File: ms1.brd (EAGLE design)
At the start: 160 x 100 mm, 119 parts, among them IC1 MAX3232EUE, J1 POWERPOLE_POWER25A, J10 Radio, J11 4-PIN-MOLEX, J12 4-PIN-MOLEX, J13 ADC2, J14 ADC2, J2 ON, J3 LED-EN, J4 RS232, J5 2-PIN-MOLEX, J6 ADC1, J7 I2C, J8 ADC2, J9 TTL_SERIAL, Q1 DMG6602SVT, Q2 DMG6602SVT, Q3 DMG6602SVT, Q4 DMG6602SVT, U1 LT1934ES6TRMPBF, U2 LT1934ES6TRMPBF, U3 DS3231SN, U4 ISL3179EIBZ, X1 KUSBVX-BS1N

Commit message: now all routed :)
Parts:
- removed C27, C29: (no value), resistor:C0805
- removed C28, C30: (no value), resistor:B/3528-21R
- removed J9: TTL_SERIAL, farnell-parts:5-MOLEX
- removed JP16, JP8: (no value), SparkFun-Passives:SJ_2S-NO
- removed L7, L8: 10mH, resistor:L3230M
- removed LED12: RADIO, led:CHIP-LED0805
- removed LED13: RADIO_EN, led:CHIP-LED0805
- removed LED14: BAT_EN, led:CHIP-LED0805
- removed LED15: SENSE_EN, led:CHIP-LED0805
- removed R30: 56, resistor:R0805
- removed R31: 100K, resistor:R0805
- removed R32, R33: 1K, resistor:R0805
- removed U$1: BUTTON_CELL_NEW, gumsense:CR2016
- removed U$2: Z1, z1:Z1
- removed U$4: TXS0108E, basestation:TSSOP20
- removed U$7: MCF0805, farnell-parts:0805
- added C17: (no value), resistor:C0805
- added C18: (no value), resistor:B/3528-21R
- added C22: 0.1uF, resistor:A/3216-18W
- added C23: 100nF, resistor:C0805
- added F1, F2, F3, F4, F5, F6, F7, F8: MCF0805, farnell-parts:0805
- added JP3: (no value), SparkFun-Passives:SJ_2S
- added JP4: (no value), jumper:JP2
- added L1: 47uH, farnell-parts:1048
- added L2: 20uH, rcl:6000-XXXX-RC
- added LED3: RAIN, led:CHIP-LED0805
- added LED4: 12V, led:CHIP-LED0805
- added LED5: 3V3, led:CHIP-LED0805
- added LED6: SENSE, led:CHIP-LED0805
- added R13: 100K, resistor:R0805
- added R15, R16: 56, resistor:R0805
- added R17: 560, resistor:R0805
- added U$8: CC1120-HEADER-SMT, CC11x:CC1120-HEADERS-SMT
- C1: value 2200uF -> 2.2uF; device rcl:E5-13 -> resistor:C0805
- C10: value 10pF -> 1uF
- C11: value 68uF -> 100nF; device rcl:PANASONIC_E -> resistor:C0805
- C12: value 330uF -> 2.2uF; device rcl:E5-8,5 -> resistor:C0805
- C13: value 100nF -> 0.22uF
- C14: value 100nF -> 10pF; device glacsweb:C0805 -> resistor:C0805
- C15: value 0.1uF -> 68uF; device resistor:A/3216-18W -> rcl:PANASONIC_E
- C16: value 0.1uF -> 330uF; device resistor:A/3216-18W -> rcl:E5-8,5
- C2: value 2.2uF -> 0.22uF
- C20: value 0.1uF -> 100nF; device resistor:A/3216-18W -> glacsweb:C0805
- C24, C25: value 100nF -> 0.1uF; device resistor:C0805 -> resistor:A/3216-18W
- C3: value 0.22uF -> 2200uF; device resistor:C0805 -> rcl:E5-13
- C5: value 1uF -> 100uF; device resistor:C0805 -> rcl:PANASONIC_E
- C6: value 100uF -> 330uF; device rcl:PANASONIC_E -> rcl:E5-8,5
- C7: value 330uF -> (none); device rcl:E5-8,5 -> resistor:C0805
- C8: value 2.2uF -> (none); device resistor:C0805 -> resistor:B/3528-21R
- C9: value 0.22uF -> 100nF
- J10: value Radio -> RS485; device farnell-parts:5-MOLEX -> farnell-parts:4-MOLEX
- J11: value 4-PIN-MOLEX -> I2C; device farnell-parts:4-MOLEX -> farnell-parts:5-MOLEX
- J12: value 4-PIN-MOLEX -> TTL_SERIAL
- J13: value ADC2 -> Radio; device farnell-parts:3-MOLEX -> farnell-parts:5-MOLEX
- J14: value ADC2 -> RS232; device farnell-parts:3-MOLEX -> farnell-parts:4-MOLEX
- J2: value ON -> RAIN
- J3: value LED-EN -> ADC1; device farnell-parts:2-MOLEX -> farnell-parts:3-MOLEX
- J4: value RS232 -> ON; device farnell-parts:5-MOLEX -> farnell-parts:2-MOLEX
- J5: value 2-PIN-MOLEX -> D1; device farnell-parts:2-MOLEX -> farnell-parts:3-MOLEX
- J6: value ADC1 -> D2
- J7: value I2C -> ADC2; device farnell-parts:5-MOLEX -> farnell-parts:3-MOLEX
- J8: value ADC2 -> LED-EN; device farnell-parts:3-MOLEX -> farnell-parts:2-MOLEX
- JP1: device SparkFun-Passives:SJ_2S -> SparkFun-Passives:SJ_2S-NO
- JP2: device jumper:JP2 -> SparkFun-Passives:SJ_2S-NO
- L3: value 47uH -> 10mH; device farnell-parts:1048 -> resistor:L3230M
- L4: value 20uH -> 10mH; device rcl:6000-XXXX-RC -> resistor:L3230M
- LED10: value SENSE -> BAT_EN
- LED11: value SENSE_5V -> SENSE_EN
- LED7: value D7 -> 5V
- LED8: value 12V -> RADIO
- LED9: value 3V3 -> RADIO_EN
- R10, R8: value 56 -> 100K
- R14, R26: value 100K -> 56
- R19: value 560 -> 56
- R2: value 100K -> 1M
- R20: value 56 -> 1M
- R21: value 56 -> 332K
- R22: value 100K -> 150
- R23: value 1M -> 56
- R24: value 332K -> 56
- R25: value 150 -> 56
- R27, R29: value 56 -> 1K
- R28: value 56 -> 47K
- R3: value 100K -> 604K
- R4: value 51K -> 100K
- R5: value 1M -> 100K
- R6: value 604K -> 100K
- R7: value 47K -> 100K
- R9: value 100K -> 51K
- U$3: value CC1120-HEADER-SMT -> BUTTON_CELL_NEW; device CC11x:CC1120-HEADERS-SMT -> gumsense:CR2016
- U$5: value MCF0805 -> Z1; device farnell-parts:0805 -> z1:Z1
- U$6: value MCF0805 -> TXS0108E; device farnell-parts:0805 -> basestation:TSSOP20
- moved J5 377.9 mm to (90.0, 95.2), turned to 180 degrees
- moved J14 348.8 mm to (77.2, 5.97)
- moved J6 346.4 mm to (90.0, 89.0), turned to 180 degrees
- moved LED11 327.7 mm to (92.5, 26.5)
- moved JP2 327.1 mm to (85.0, 78.4), turned to 180 degrees
- moved U$6 324.4 mm to (64.4, 16.3), turned to 90 degrees
- moved J12 315.8 mm to (66.0, 5.97)
- moved U4 314.1 mm to (89.3, 17.9), turned to 270 degrees
- moved LED1 309.9 mm to (96.9, 94.7), turned to 180 degrees
- moved LED2 303.4 mm to (96.9, 88.8)
- moved C20 301.7 mm to (96.0, 17.7), turned to 90 degrees
- moved J8 297.2 mm to (55.0, 6.10)
- moved R7 292.7 mm to (55.9, 21.0), turned to 180 degrees
- moved C14 292.4 mm to (72.4, 68.7)
- moved C21 291.5 mm to (82.3, 16.1), turned to 270 degrees
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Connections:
- new net N$11: F4.1, J12.4
- new net N$18: F1.2, J3.1
- new net N$19: F2.2, J7.1
- new net N$21: F7.2, J6.1
- new net N$22: F8.2, J5.1
- net 232_RX: now also U$6.3; no longer U$4.3
- net 232_TX: now also U$6.6; no longer U$4.6
- net 323_3V3: now also C23.2, JP4.3; no longer C19.2, JP2.3
- net 485_3V3: now also C20.1, JP4.1, R27.2; no longer C14.1, JP2.1, R32.2
- net 485_RX: now also U$6.1; no longer U$4.1
- net 485_TX: now also U$6.5; no longer U$4.5
- net ADC_1: now also J3.2, U$5.A16; no longer J6.2, U$2.A16
- net ADC_2: now also J7.2, U$5.A9; no longer J8.2, U$2.A9
- net ADC_3V3: now also U$5.A14, U$5.A4; no longer U$2.A14, U$2.A4
- net ADC_7: now also C10.1, R8.1, R9.2, U$5.A6; no longer C5.1, R3.1, R4.2, U$2.A6
- net AGND: now also C10.2, J3.3, J7.3, R9.1, U$5.A1, U$5.A11, U$5.A12, U$5.A2; no longer C5.2, J6.3, J8.3, R4.1, U$2.A1, U$2.A11, U$2.A12, U$2.A2
- net BATV_EN: now also JP3.2, R25.2, R4.2; no longer JP1.2, R1.2, R29.2
- net DC_IN: now also J4.2, R5.2; no longer J2.2, R2.2
- net DIO_1: now also J5.2, R14.2, U$5.C51; no longer J13.2, R8.2, U$2.C46, U$2.C51
- net DIO_2: now also J6.2, R15.2, U$5.C46; no longer J14.2, R10.2
- net GND: now also C1.2, C12.2, C15.-, C16.-, C17.2, C18.-, C20.2, C23.1, C24.-, C25.+, C3.-, C5.-, C7.2, C8.-, C9.2, J10.1, J14.1, J5.3, J6.3, J8.1, L4.2, R10.1, R21.1, R3.1, R4.1, U$3.GND, U$5.B24, U$5.C39, U$6.11; no longer C1.-, C11.-, C12.-, C13.1, C14.2, C2.2, C20.-, C21.+, C24.2, C27.2, C28.-, C29.2, C30.-, C7.-, C8.2, J13.3, J14.3, J3.1, J4.1, J7.1, J9.1, L8.2, R22.1, R24.1, R31.1, R9.1, U$1.GND, U$2.B24, U$2.C39, U$4.11
- net LGND: now also J8.2, LED3.C, LED4.C, LED5.C, LED6.C; no longer J3.2, LED12.C, LED13.C, LED14.C, LED15.C
- net N$1: now also J4.1; no longer J2.1
- net N$10: now also R27.1; no longer R32.1
- net N$107: now also C5.+, L1.2, L2.1, R2.2; no longer C6.+, L3.2, L4.1, R5.2
- net N$108: now also LED8.A, R23.1; no longer LED12.A, R27.1
- net N$109: now also LED7.A, R22.1; no longer LED11.A, R25.1
- net N$110: now also LED6.A, R19.1; no longer LED10.A, R21.1
- net N$111: now also LED5.A, R18.1; no longer LED9.A, R20.1
- net N$117: now also C2.1; no longer C3.1
- net N$118: now also R2.1, R3.2; no longer R5.1, R6.2
- net N$12: now also R5.1; no longer R2.1
- net N$13: now also C6.+, C7.1, C8.+, JP1.2, L2.2; no longer C29.1, C30.+, C7.+, JP16.2, L4.2
- net N$14: now also C16.+, C17.1, C18.+, JP2.1; no longer C12.+, C27.1, C28.+, JP8.1
- net N$15: now also LED9.A, R24.1; no longer LED13.A, R28.1
- net N$16: now also LED3.A, R16.1; no longer LED7.A, R18.1
- net N$17: now also F6.1, J14.4; no longer J12.4, U$6.1
- net N$2: now also LED4.A, R17.1; no longer LED8.A, R19.1
- net N$20: now also R15.1; no longer R10.1
- net N$23: now also R14.1; no longer R8.1
- net N$24: now also C9.1, L3.2, Q2.P$4; no longer C24.1, L7.2, Q3.P$4
- net N$25: now also Q3.P$3, Q3.P$6; no longer Q2.P$3, Q2.P$6
- net N$26: now also F3.1, J2.1; no longer J5.1, U$7.1
- net N$3: now also C13.2; no longer C9.2
- net N$4: now also C13.1; no longer C9.1
- net N$5: now also C14.2, R20.1, R21.2; no longer C10.2, R23.1, R24.2
- net N$50: now also LED10.A, R25.1; no longer LED14.A, R29.1
- net N$51: now also LED11.A, R26.1; no longer LED15.A, R30.1
- net N$59: now also C22.-; no longer C16.-
- net N$6: now also C14.1, C15.+, R20.2; no longer C10.1, C11.+, R23.2
- net N$7: now also Q2.P$3, Q2.P$6, R7.1; no longer Q3.P$3, Q3.P$6, R14.1
- net N$70: now also R13.1; no longer R26.1
- net N$78: now also C2.2, L1.1; no longer C3.2, L3.1
- net N$8: now also R28.1, U$6.10; no longer R7.1, U$4.10
- net N$80: now also C22.+; no longer C16.+
- net N$81: now also C21.-; no longer C15.-
- net N$85: now also C21.+; no longer C15.+
- net N$86: now also C24.+; no longer C20.+
- net N$87: now also C25.-; no longer C21.-
- net N$9: now also F5.1, J10.4; no longer J11.4, U$5.1
- net RADIO_!RST: now also R29.1, U$5.C43, U$8.RESET; no longer R33.1, U$2.C43, U$3.RESET
- net RADIO_3V3: now also C11.1, L3.1, R23.2, R29.2, U$8.3V3-1, U$8.3V3-2; no longer C25.1, L7.1, R27.2, R33.2, U$3.3V3-1, U$3.3V3-2
- net RADIO_CCA_STATUS: now also U$5.C42, U$8.GPIO3; no longer U$2.C42, U$3.GPIO3
- net RADIO_CSN: now also J13.2, U$5.C48, U$8.CSN; no longer J10.2, U$2.C48, U$3.CSN
- net RADIO_EN: now also Q2.P$1, R24.2, R6.2, U$5.B30; no longer Q3.P$1, R12.2, R28.2, U$2.B30
- net RADIO_INT: now also J13.1, U$5.C54, U$8.GPIO0; no longer J10.1, U$2.C54, U$3.GPIO0
- net RAIN: now also J2.2, R1.2, R16.2, U$5.C49; no longer J5.2, R18.2, R31.2, U$2.C49
- net RGND: now also C11.2, L4.1, U$8.GND, U$8.GND1, U$8.GND2; no longer C25.2, L8.1, U$3.GND, U$3.GND1, U$3.GND2
- net RS232_RXD: now also J14.2; no longer J12.2, J4.2
- net RS232_TXD: now also J14.3; no longer J12.3, J4.3
- net RS485_N: now also J10.2; no longer J11.2
- net RS485_P: now also J10.3; no longer J11.3
- net SCL: now also J11.3, U$5.B26; no longer J7.3, U$2.B26
- net SDA: now also J11.2, U$5.B28; no longer J7.2, U$2.B28
- net SENSE_3V3: now also F1.1, F2.1, F7.1, F8.1, J11.4, JP4.2, R19.2, R28.2, U$6.2; no longer J13.1, J14.1, J4.4, J6.1, J7.4, J8.1, J9.4, JP2.2, R21.2, R7.2, U$4.2
- net SENSE_5V: now also F4.2, F5.2, F6.2, J11.5, JP2.2, R22.2; no longer J4.5, J7.5, J9.5, JP8.2, R25.2, U$5.2, U$6.2
- net SENSE_EN: now also JP3.1, Q3.P$1, R10.2, R12.2, R26.2, U$5.B32; no longer JP1.1, Q2.P$1, R22.2, R30.2, R9.2, U$2.B32
- net SPI_CLK: now also J13.3, U$5.B34, U$8.SCLK; no longer J10.3, U$2.B34, U$3.SCLK
- net SPI_SIMO: now also J13.4, U$5.B36, U$8.MOSI; no longer J10.4, U$2.B36, U$3.MOSI
- net SPI_SOMI: now also J13.5, U$5.B40, U$8.MISO; no longer J10.5, U$2.B40, U$3.MISO
- net TTL_RX: now also J12.2, U$6.4; no longer J9.2, U$4.4
- net TTL_TX: now also J12.3, U$6.7; no longer J9.3, U$4.7
- net UART0_RX: now also U$5.B35; no longer U$2.B35
- net UART0_TX: now also U$5.B37; no longer U$2.B37
- net UART1_RX: now also U$5.B31, U$6.17, U$6.18, U$6.20; no longer U$2.B31, U$4.17, U$4.18, U$4.20
- net UART1_TX: now also U$5.B33, U$6.14, U$6.15, U$6.16; no longer U$2.B33, U$4.14, U$4.15, U$4.16
- net USB_D_N: now also U$5.B21; no longer U$2.B21
- net USB_D_P: now also U$5.B19; no longer U$2.B19
- net USB_GND: now also U$5.B17; no longer U$2.B17
- net USB_VCC: now also U$5.A13, U$5.A3, U$5.B23; no longer U$2.A13, U$2.A3, U$2.B23
- net VBAT_B: now also U$3.V+@1, U$3.V+@2; no longer U$1.V+@1, U$1.V+@2
- net VCC: now also C1.1, C3.+, Q3.P$2, R17.2; no longer C1.+, C2.1, Q2.P$2, R19.2
- net VCC_3V3: now also C19.2, F3.2, JP1.1, Q2.P$2, R13.2, R18.2, R7.2, U$5.B22, U$5.C40, U$6.19; no longer C13.2, JP16.1, Q3.P$2, R14.2, R20.2, R26.2, U$2.B22, U$2.C40, U$4.19, U$7.2
- net VCC_HP2_SW: now also C12.1, Q3.P$4; no longer C8.1, Q2.P$4
- net VCC_HP2_SW1: now also R8.2; no longer R3.2
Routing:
- net LGND: track 39.3 -> 378.6 mm, vias 2 -> 8
- net DIO_1: track 0.00 -> 119.0 mm, vias 0 -> 1
- net RAIN: track 0.00 -> 117.7 mm, vias 0 -> 1
- net DIO_2: track 0.00 -> 106.0 mm, vias 0 -> 1
- net AGND: track 0.00 -> 86.9 mm, vias 0 -> 1
- net SENSE_EN: track 222.9 -> 152.6 mm
- net ADC_1: track 0.00 -> 64.5 mm, vias 0 -> 1
- net ADC_2: track 0.00 -> 59.9 mm, vias 0 -> 1
- net VCC_3V3: track 162.2 -> 221.6 mm, vias 3 -> 8
- net UART1_RX: track 0.00 -> 47.1 mm, vias 0 -> 1
- net UART1_TX: track 0.00 -> 38.6 mm, vias 0 -> 1
- net 485_3V3: track 5.39 -> 42.9 mm, vias 0 -> 1
- net 485_RX: track 0.00 -> 33.3 mm, vias 0 -> 2
- net SENSE_3V3: track 297.9 -> 331.0 mm, vias 1 -> 2
- net VCC: track 151.2 -> 118.6 mm
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- removed copper zone on layer 1, net AGND
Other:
- board size 160 x 100 mm -> 100 x 100 mm

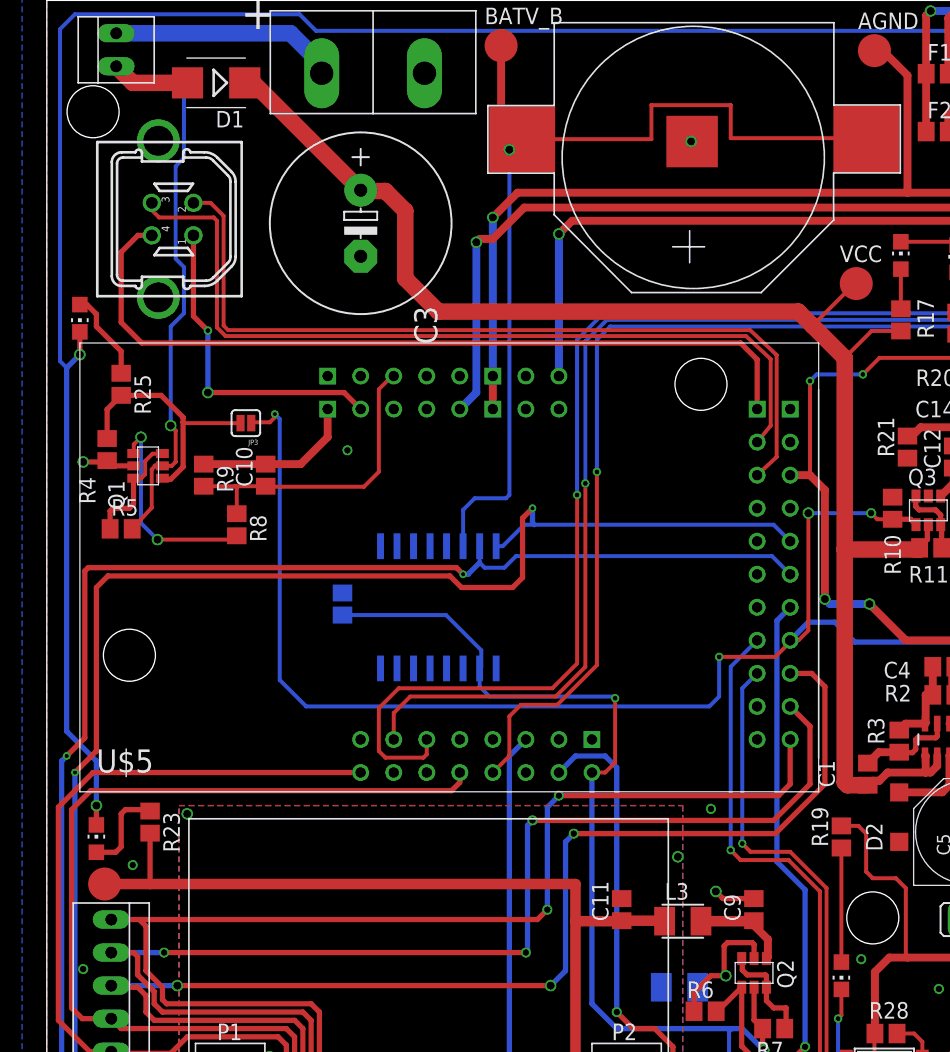
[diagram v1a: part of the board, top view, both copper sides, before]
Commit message: A couple of small bugfixes
Moved battery + away from battery negative terminal
moved clearance issue via
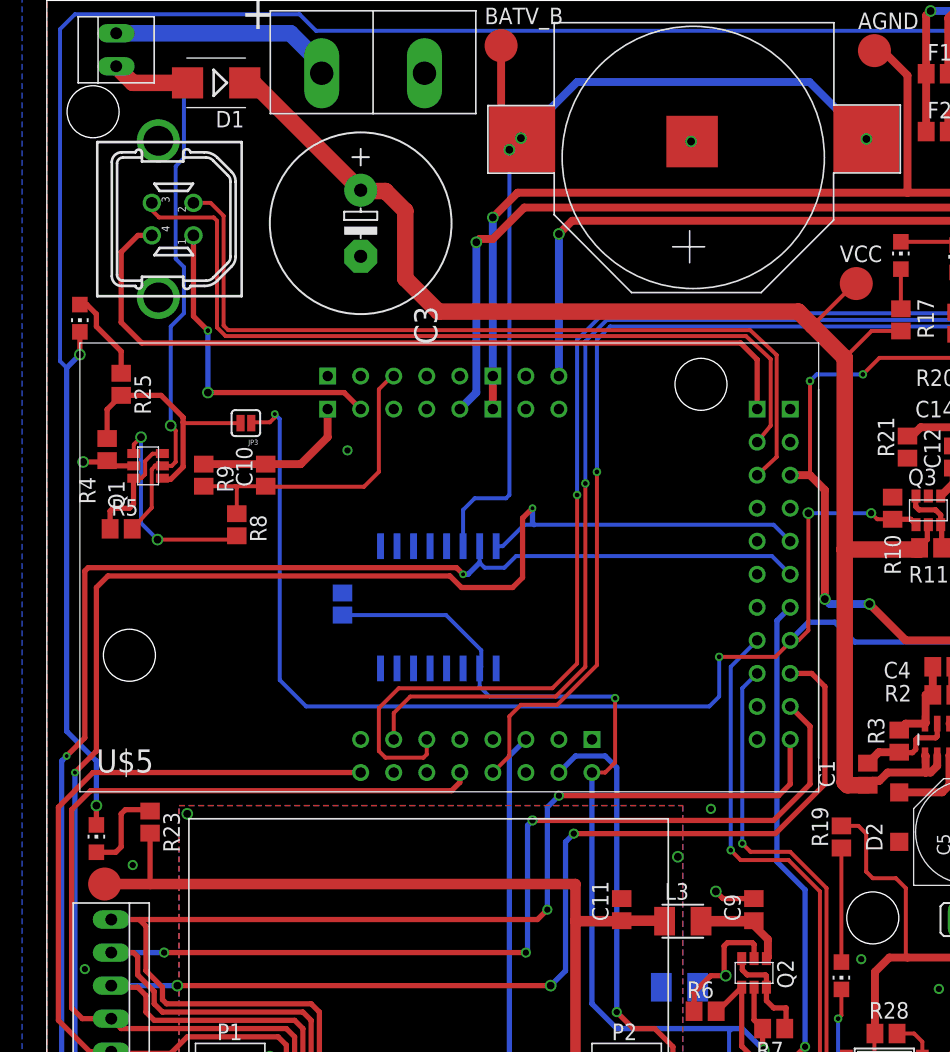
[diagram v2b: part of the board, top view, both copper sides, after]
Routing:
- net VBAT_B: track 75.4 -> 74.0 mm, vias 1 -> 3
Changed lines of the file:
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@@
 <?xml version="1.0" encoding="utf-8"?>
 <!DOCTYPE eagle SYSTEM "eagle.dtd">
-<eagle version="6.5.0">
+<eagle version="6.4">
 <drawing>
 <settings>
@@
 <contactref element="R4" pad="1"/>
 <contactref element="Q1" pad="P$5"/>
-<contactref element="U$5" pad="B24" route="any" routetag="G$1.DGND"/>
-<contactref element="U$5" pad="C39" route="any" routetag="G$1.DGND"/>
+<contactref element="U$5" pad="B24" route="any" routetag="DGND"/>
+<contactref element="U$5" pad="C39" route="any" routetag="DGND"/>
 <contactref element="U3" pad="5"/>
 <contactref element="U3" pad="7"/>
@@
 <via x="23.114" y="65.405" extent="1-16" drill="0.4826" shape="square"/>
 <via x="51.054" y="37.846" extent="1-16" drill="0.4826" shape="square"/>
-<via x="2.794" y="25.527" extent="1-16" drill="0.4826" shape="square"/>
+<via x="2.921" y="25.527" extent="1-16" drill="0.4826" shape="square"/>
 <via x="6.604" y="33.528" extent="1-16" drill="0.4826" shape="square"/>
 <via x="64.897" y="18.161" extent="1-16" drill="0.4826" shape="square"/>
@@
 <contactref element="R13" pad="2"/>
 <contactref element="R18" pad="2"/>
-<contactref element="U$5" pad="B22" route="any" routetag="G$1.D-3V"/>
-<contactref element="U$5" pad="C40" route="any" routetag="G$1.D-3V"/>
+<contactref element="U$5" pad="B22" route="any" routetag="D-3V"/>
+<contactref element="U$5" pad="C40" route="any" routetag="D-3V"/>
 <contactref element="U3" pad="2"/>
 <contactref element="C19" pad="2"/>
@@
 <contactref element="U3" pad="14"/>
 <wire x1="63.008" y1="89.348" x2="63.754" y2="89.348" width="0.3048" layer="1"/>
-<wire x1="36.543" y1="89.3305" x2="46.482" y2="89.3305" width="0.3048" layer="1"/>
-<wire x1="46.482" y1="89.3305" x2="46.482" y2="91.948" width="0.3048" layer="1"/>
-<wire x1="46.482" y1="91.948" x2="52.578" y2="91.948" width="0.3048" layer="1"/>
-<wire x1="52.578" y1="91.948" x2="52.578" y2="89.408" width="0.3048" layer="1"/>
-<wire x1="52.578" y1="89.408" x2="63.008" y2="89.408" width="0.3048" layer="1"/>
-<wire x1="63.008" y1="89.408" x2="63.008" y2="89.348" width="0.3048" layer="1"/>
 <wire x1="36.543" y1="89.3305" x2="36.3715" y2="89.3305" width="0.3048" layer="1"/>
 <wire x1="36.3715" y1="89.3305" x2="35.56" y2="88.519" width="0.3048" layer="1"/>
@@
 <wire x1="34.925" y1="96.52" x2="34.925" y2="89.154" width="0.6096" layer="1"/>
 <wire x1="34.925" y1="89.154" x2="35.56" y2="88.519" width="0.6096" layer="1"/>
+<wire x1="36.543" y1="89.3305" x2="36.4655" y2="89.408" width="0.4064" layer="1"/>
+<wire x1="36.4655" y1="89.408" x2="36.449" y2="89.408" width="0.4064" layer="1"/>
+<via x="36.449" y="89.408" extent="1-16" drill="0.6" shape="square"/>
+<wire x1="36.449" y1="89.408" x2="40.767" y2="93.726" width="0.6096" layer="16"/>
+<wire x1="40.767" y1="93.726" x2="58.63" y2="93.726" width="0.6096" layer="16"/>
+<wire x1="58.63" y1="93.726" x2="63.008" y2="89.348" width="0.6096" layer="16"/>
+<via x="63.008" y="89.348" extent="1-16" drill="0.6" shape="square"/>
 </signal>
 <signal name="N$7">
@@
 <contactref element="C10" pad="2"/>
 <contactref element="R9" pad="1"/>
-<contactref element="U$5" pad="A1" route="any" routetag="G$1.AGND"/>
-<contactref element="U$5" pad="A2" route="any" routetag="G$1.AGND"/>
-<contactref element="U$5" pad="A11" route="any" routetag="G$1.AGND"/>
-<contactref element="U$5" pad="A12" route="any" routetag="G$1.AGND"/>
+<contactref element="U$5" pad="A1" route="any" routetag="AGND"/>
+<contactref element="U$5" pad="A2" route="any" routetag="AGND"/>
+<contactref element="U$5" pad="A11" route="any" routetag="AGND"/>
+<contactref element="U$5" pad="A12" route="any" routetag="AGND"/>
 <contactref element="AGND" pad="TP"/>
 <contactref element="J3" pad="3"/>
@@
 </signal>
 <signal name="USB_VCC">
-<contactref element="U$5" pad="A3" route="any" routetag="G$1.USB-5V"/>
-<contactref element="U$5" pad="A13" route="any" routetag="G$1.USB-5V"/>
-<contactref element="U$5" pad="B23" route="any" routetag="G$1.USB-5V"/>
+<contactref element="U$5" pad="A3" route="any" routetag="USB-5V"/>
+<contactref element="U$5" pad="A13" route="any" routetag="USB-5V"/>
+<contactref element="U$5" pad="B23" route="any" routetag="USB-5V"/>
 <contactref element="X1" pad="1"/>
 <wire x1="11.2725" y1="81.935" x2="11.2725" y2="75.7225" width="0.4064" layer="1"/>
@@
 </signal>
 <signal name="ADC_3V3">
-<contactref element="U$5" pad="A4" route="any" routetag="G$1.ADC_3V3"/>
-<contactref element="U$5" pad="A14" route="any" routetag="G$1.ADC_3V3"/>
+<contactref element="U$5" pad="A4" route="any" routetag="ADC_3V3"/>
+<contactref element="U$5" pad="A14" route="any" routetag="ADC_3V3"/>
 </signal>
 <signal name="VCC-3V">

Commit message: silk screen worked
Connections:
- removed net 323_3V3: C23.2, IC1.16, JP4.3
- new net 232_3V3: C23.2, IC1.16, JP4.1
- net 485_3V3: now also JP4.3; no longer JP4.1
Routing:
- net 323_3V3: track 17.4 -> 0.00 mm, vias 2 -> 0
- net 232_3V3: track 0.00 -> 15.9 mm, vias 0 -> 1
- net 485_3V3: track 42.9 -> 37.3 mm, vias 1 -> 0
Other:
- board text added: "232"
- board text added: "485"
- board text added: "MS1"
- board text added: "PJB"
- board text added: "TW"
- board text added: "V0.1"
